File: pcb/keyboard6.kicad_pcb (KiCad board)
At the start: 2 copper layers, 149.9 x 129.4 mm, 74 parts, among them J1 AudioJack4, J2 USB_B_Micro, SW1 SW_DIP_x01, SW10 SW_DIP_x01, SW11 SW_DIP_x01, SW12 SW_DIP_x01, SW13 SW_DIP_x01, SW14 SW_DIP_x01, SW15 SW_DIP_x01, SW16 SW_DIP_x01, SW17 SW_DIP_x01, SW18 SW_DIP_x01, SW19 SW_DIP_x01, SW2 SW_DIP_x01, SW20 SW_DIP_x01, SW21 SW_DIP_x01, SW22 SW_DIP_x01, SW23 SW_DIP_x01, SW24 SW_DIP_x01, SW25 SW_DIP_x01, SW26 SW_DIP_x01, SW27 SW_DIP_x01, SW28 SW_DIP_x01, SW29 SW_DIP_x01, SW3 SW_DIP_x01, SW30 SW_Push_Dual, SW4 SW_DIP_x01, SW5 SW_DIP_x01, SW6 SW_DIP_x01, SW7 SW_DIP_x01, SW8 SW_DIP_x01, SW9 SW_DIP_x01, Y1 16MHz

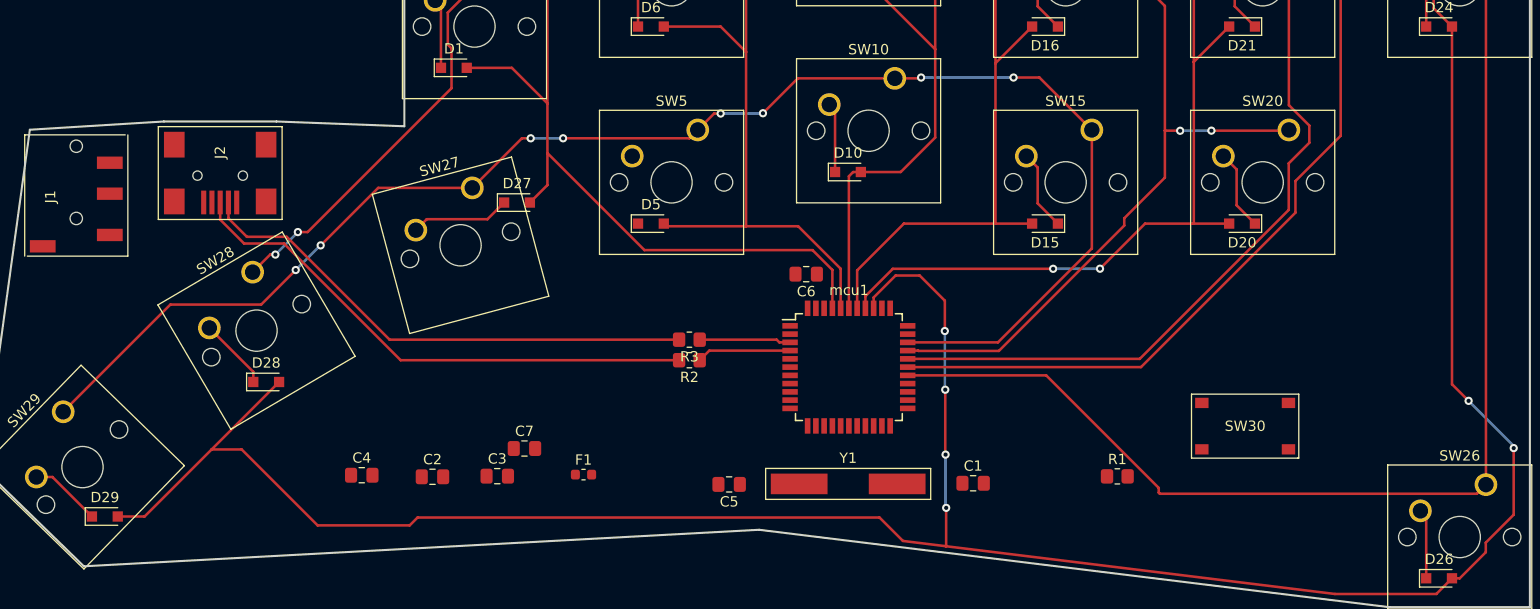
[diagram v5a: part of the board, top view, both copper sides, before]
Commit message: Moving mcu closer to connectors.
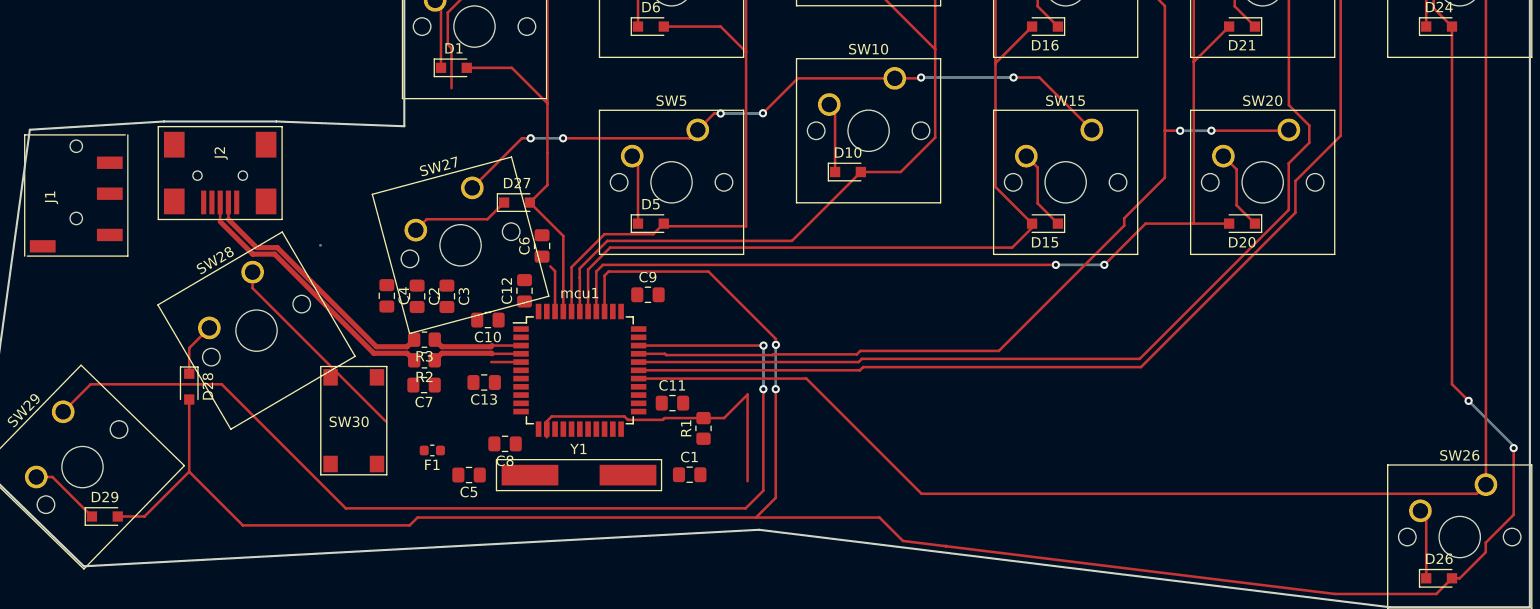
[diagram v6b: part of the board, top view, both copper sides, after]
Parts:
- added C10: 0.1u, Capacitor_SMD:C_0805_2012Metric_Pad1.18x1.45mm_HandSolder, F.Cu at (1.30, 9.35)
- added C11: 0.1u, Capacitor_SMD:C_0805_2012Metric_Pad1.18x1.45mm_HandSolder, F.Cu at (19.2, 17.4)
- added C12: 0.1u, Capacitor_SMD:C_0805_2012Metric_Pad1.18x1.45mm_HandSolder, F.Cu at (4.85, 6.51)
- added C13: 0.1u, Capacitor_SMD:C_0805_2012Metric_Pad1.18x1.45mm_HandSolder, F.Cu at (0.94, 15.4)
- added C8: 0.1u, Capacitor_SMD:C_0805_2012Metric_Pad1.18x1.45mm_HandSolder, F.Cu at (2.96, 21.4)
- added C9: 0.1u, Capacitor_SMD:C_0805_2012Metric_Pad1.18x1.45mm_HandSolder, F.Cu at (16.8, 6.90)
- SW30: footprint keyboard6:C_K_PTS641SP31SMTR2LFS -> keyboard6:SW_E_SW_TL_3303
- moved SW30 86.4 mm to (-11.7, 19.1), turned to 180 degrees
- moved R1 40.4 mm to (22.2, 19.9), turned to 90 degrees
- moved C1 27.5 mm to (20.9, 24.3)
- moved Y1 26.1 mm to (10.1, 24.4)
- moved mcu1 26.1 mm to (10.2, 14.2)
- moved C6 25.7 mm to (6.55, 2.16), turned to 90 degrees
- moved R2 25.7 mm to (-4.85, 13.2)
- moved R3 25.7 mm to (-4.85, 11.2)
- moved C5 25.2 mm to (-0.53, 24.4)
- moved C3 18.1 mm to (-2.67, 7.05), turned to 270 degrees
- moved C4 17.6 mm to (-8.50, 7.00), turned to 270 degrees
- moved C2 17.6 mm to (-5.56, 7.05), turned to 270 degrees
- moved F1 14.8 mm to (-4.09, 22.0), turned to 180 degrees
- moved C7 11.5 mm to (-4.89, 15.7), turned to 180 degrees
- moved D28 7.47 mm to (-27.6, 15.8), turned to 270 degrees
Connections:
- net Net-(J2-Pad2) renamed /Controller/USB_FULL1_N
- net Net-(J2-Pad3) renamed /Controller/USB_FULL1_P
- net Net-(R2-Pad1) renamed /Controller/USB_FULL_P
- net Net-(R3-Pad1) renamed /Controller/USB_FULL_N
- C2 pad 1: Net-(C2-Pad1) -> UVCC
- C3 pad 1: Net-(C2-Pad1) -> UVCC
- C4 pad 1: Net-(C2-Pad1) -> UVCC
- F1 pad 1: VBUS -> UVCC
- F1 pad 2: Net-(C2-Pad1) -> /Controller/VBUS
- J1 pad T: VBUS -> UVCC
- J2 pad 1: Net-(C2-Pad1) -> /Controller/VBUS
- R1 pad 1: VBUS -> UVCC
- mcu1 pad 12: Net-(mcu1-Pad12) -> Net-(J1-PadR1)
- mcu1 pad 14: VBUS -> UVCC
- mcu1 pad 2: VBUS -> UVCC
- mcu1 pad 20: Net-(J1-PadR1) -> Net-(mcu1-Pad20)
- mcu1 pad 24: VBUS -> UVCC
- mcu1 pad 34: VBUS -> UVCC
- mcu1 pad 44: VBUS -> UVCC
- mcu1 pad 7: VBUS -> UVCC
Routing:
- net Net-(R1-Pad2): track 0.00 -> 30.8 mm
- net /Controller/col2: track 115.9 -> 143.2 mm
- net /Controller/col1: track 107.8 -> 134.8 mm
- net /Controller/USB_FULL1_P: track 51.8 -> 26.2 mm
- net /Controller/row2: track 184.8 -> 210.2 mm
- net /Controller/row1: track 203.3 -> 228.7 mm
- net /Controller/USB_FULL1_N: track 50.1 -> 25.0 mm
- net /Controller/col5: track 141.0 -> 116.1 mm
- net /Controller/row0: track 254.6 -> 279.5 mm
- net /Controller/col3: track 129.3 -> 149.7 mm
- net /Controller/row3: track 175.0 -> 193.6 mm, vias 10 -> 8
- net /Controller/row4: track 148.3 -> 166.7 mm
- net Net-(D5-Pad1): track 0.00 -> 6.77 mm
- net GND1: track 0.00 -> 5.85 mm
- net /Controller/col0: track 259.7 -> 262.2 mm, vias 6 -> 4
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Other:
- net class USB_FULL added: clearance 0.127, trace_width 0.25, via_dia 0.8, via_drill 0.4
- net class USB_PWR added: clearance 0.4, trace_width 0.3, via_dia 0.8, via_drill 0.4

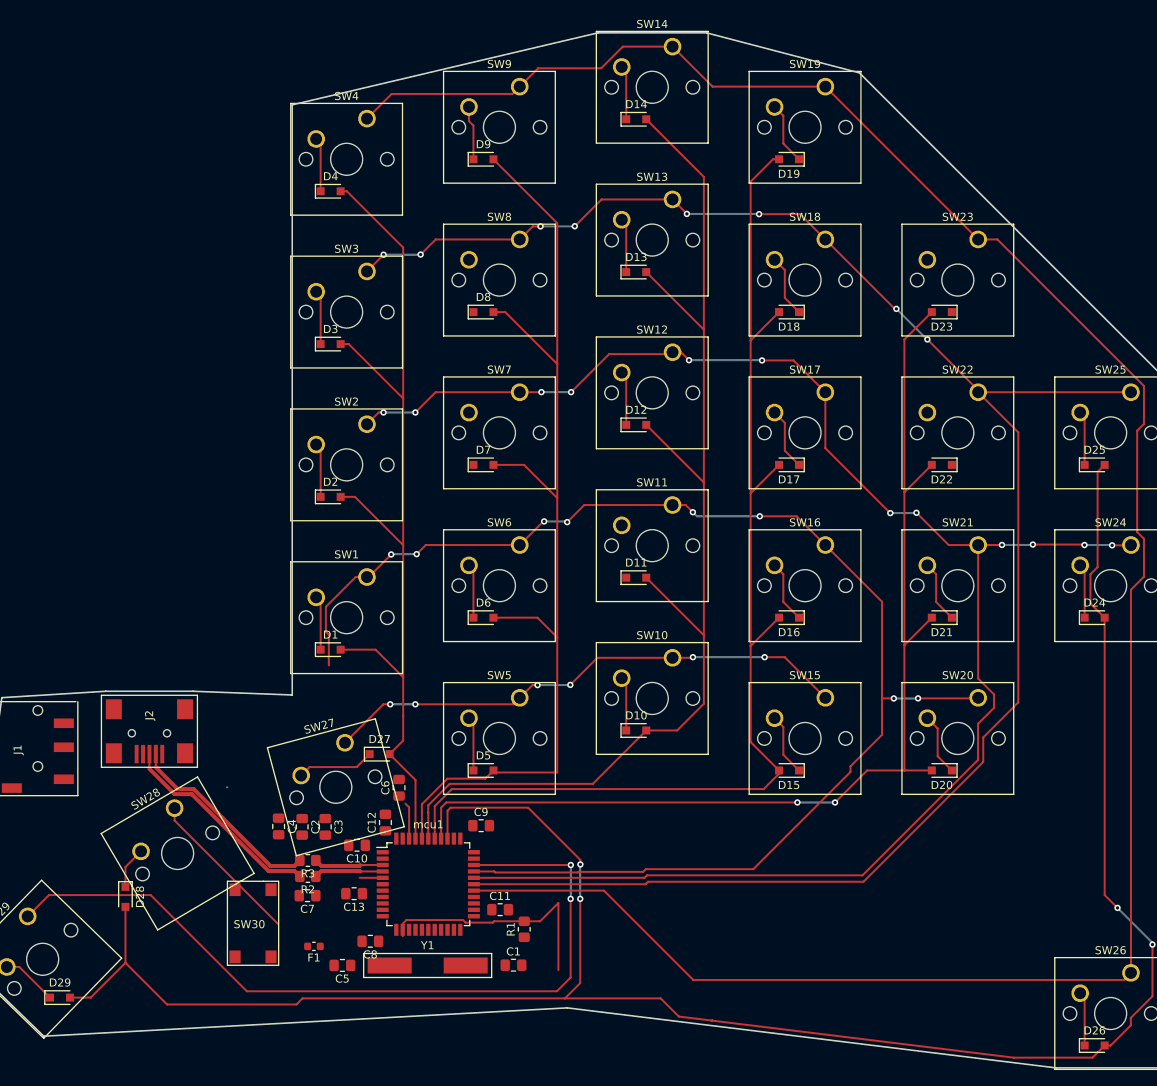
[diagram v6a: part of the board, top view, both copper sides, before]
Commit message: Power and signals routed.
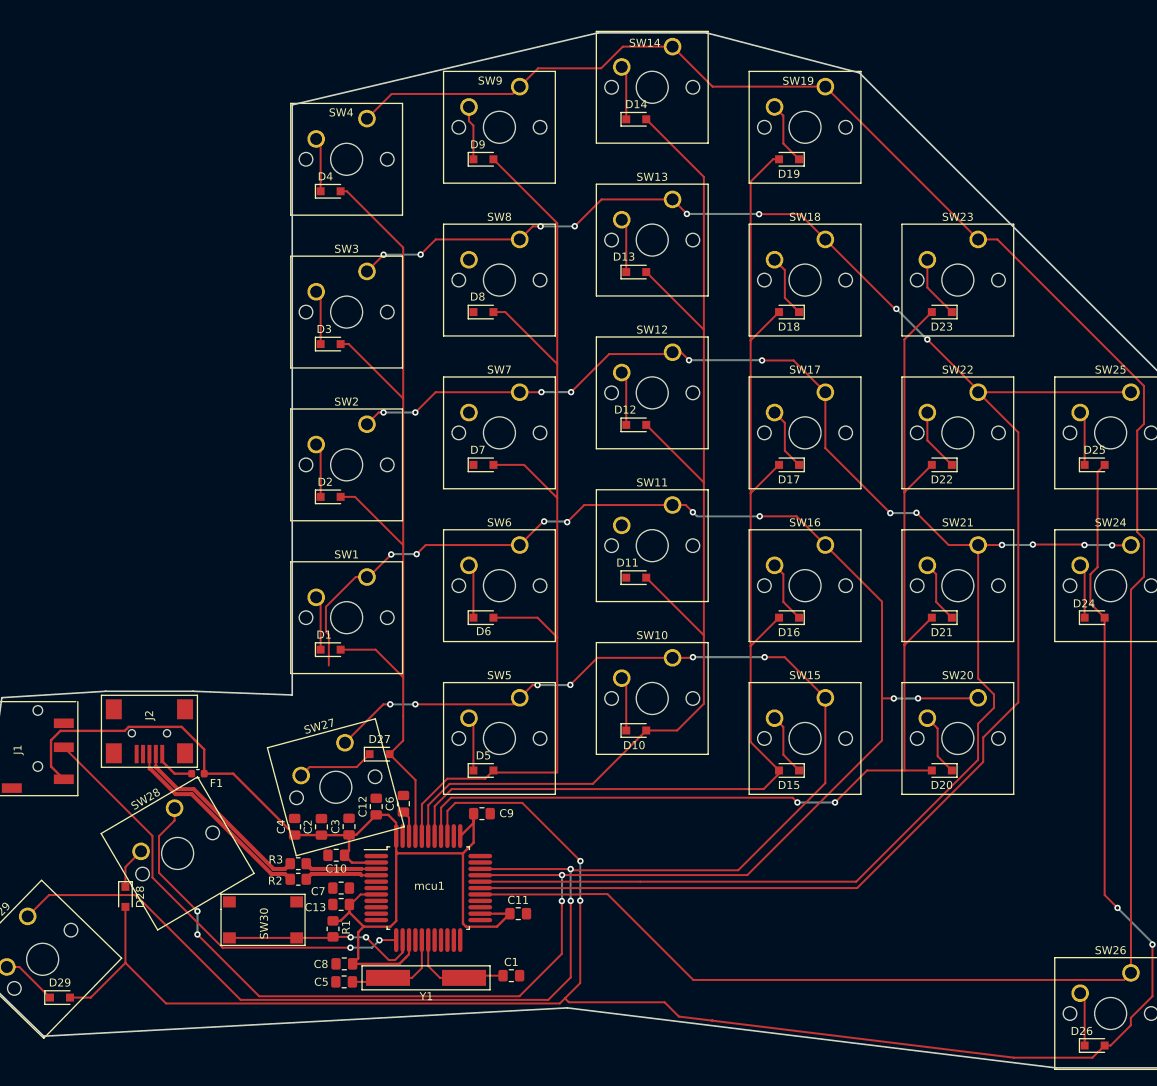
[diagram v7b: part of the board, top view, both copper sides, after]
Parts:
- mcu1: footprint Package_QFP:TQFP-44_10x10mm_P0.8mm -> keyboard6:QFP-44_10x10_Pitch0.8mm_Hand_solder
- moved F1 26.0 mm to (-18.6, 0.40)
- moved R1 23.9 mm to (-1.70, 19.8), turned to 270 degrees
- moved C8 4.31 mm to (-0.29, 24.2)
- moved C7 4.31 mm to (-0.69, 14.7)
- moved C3 2.97 mm to (0.30, 7.01), turned to 90 degrees
- moved C10 2.88 mm to (-1.30, 10.6)
- moved C2 2.41 mm to (-3.15, 7.05), turned to 90 degrees
- moved C11 2.32 mm to (21.4, 17.9)
- moved C12 2.31 mm to (3.70, 4.51)
- moved C13 2.11 mm to (-0.69, 16.8)
- moved C6 2.07 mm to (7.10, 4.16)
- moved C5 2.07 mm to (-0.31, 26.4)
- moved C4 2.00 mm to (-6.50, 7.04), turned to 90 degrees
- moved Y1 1.56 mm to (9.93, 25.9)
- moved C9 1.50 mm to (16.9, 5.40)
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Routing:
- net UVCC: track 0.00 -> 143.5 mm
- net /Controller/row3: track 193.6 -> 253.3 mm, vias 8 -> 12
- net Net-(J1-PadR1): track 0.00 -> 55.4 mm, vias 0 -> 2
- net /Controller/row4: track 166.7 -> 214.1 mm
- net Net-(C1-Pad1): track 0.00 -> 13.3 mm
- net Net-(C5-Pad1): track 0.00 -> 12.9 mm
- net Net-(D23-Pad1): track 0.00 -> 7.81 mm
- net Net-(D22-Pad1): track 0.00 -> 7.81 mm
- net Net-(R1-Pad2): track 30.8 -> 24.9 mm, vias 0 -> 2
- net GND1: track 5.85 -> 0.00 mm
- net /Controller/VBUS: track 0.00 -> 5.22 mm
- net Net-(C6-Pad1): track 0.00 -> 3.29 mm
- net /Controller/USB_FULL_P: track 7.87 -> 9.09 mm
- net /Controller/USB_FULL_N: track 7.89 -> 9.03 mm
- net /Controller/USB_FULL1_N: track 25.0 -> 24.0 mm
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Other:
- net class Default: clearance 0.4 -> 0.2
- net class USB_PWR: clearance 0.4 -> 0.2
- rule trace_clearance: 0.4 -> 0.2
